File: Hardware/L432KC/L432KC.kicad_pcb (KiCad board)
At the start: 2 copper layers, 64.8 x 55.9 mm, 26 parts, among them J1 Conn_01x09, J2 Conn_01x07, J3 USB_B_Micro, J4 JVCC, J5 JTAG, J6 LogicAna, U1 NUCLEO-L432KC

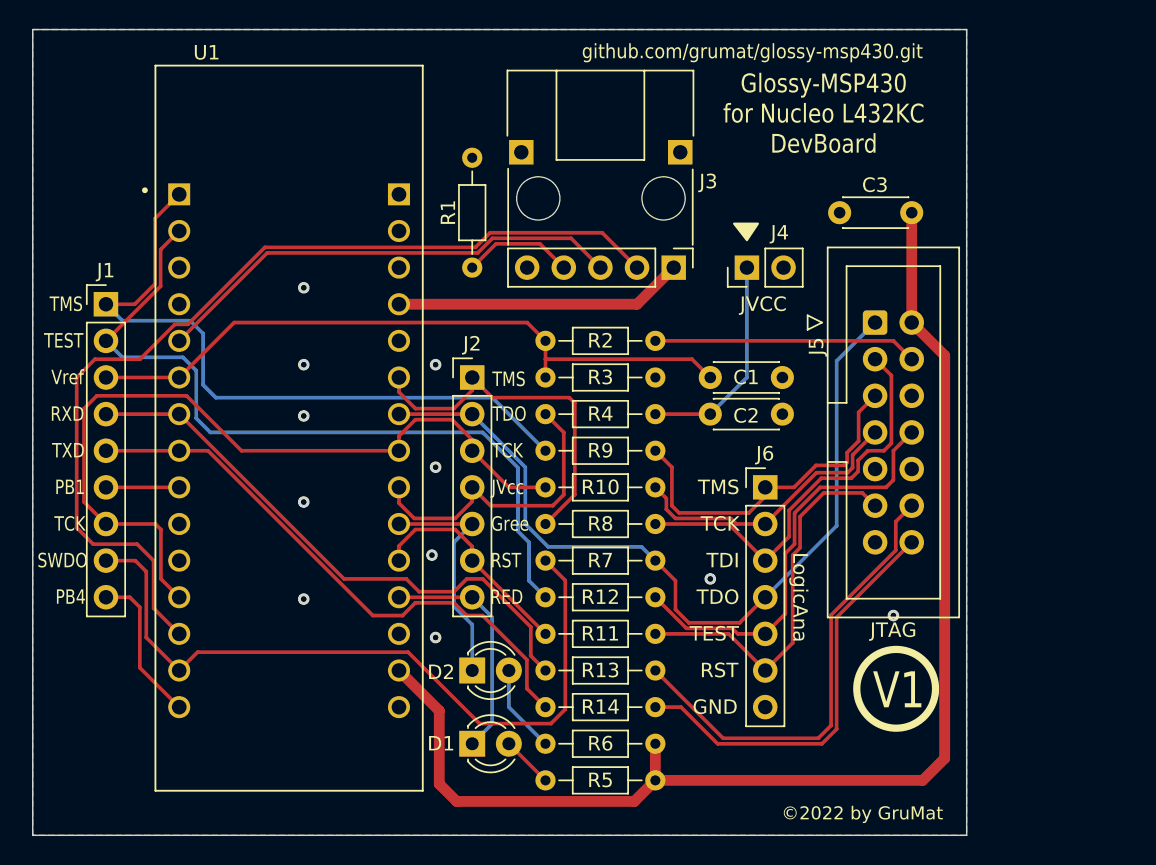
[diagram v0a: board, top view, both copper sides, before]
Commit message: Update Hardware models - Added dual support for L432KC.
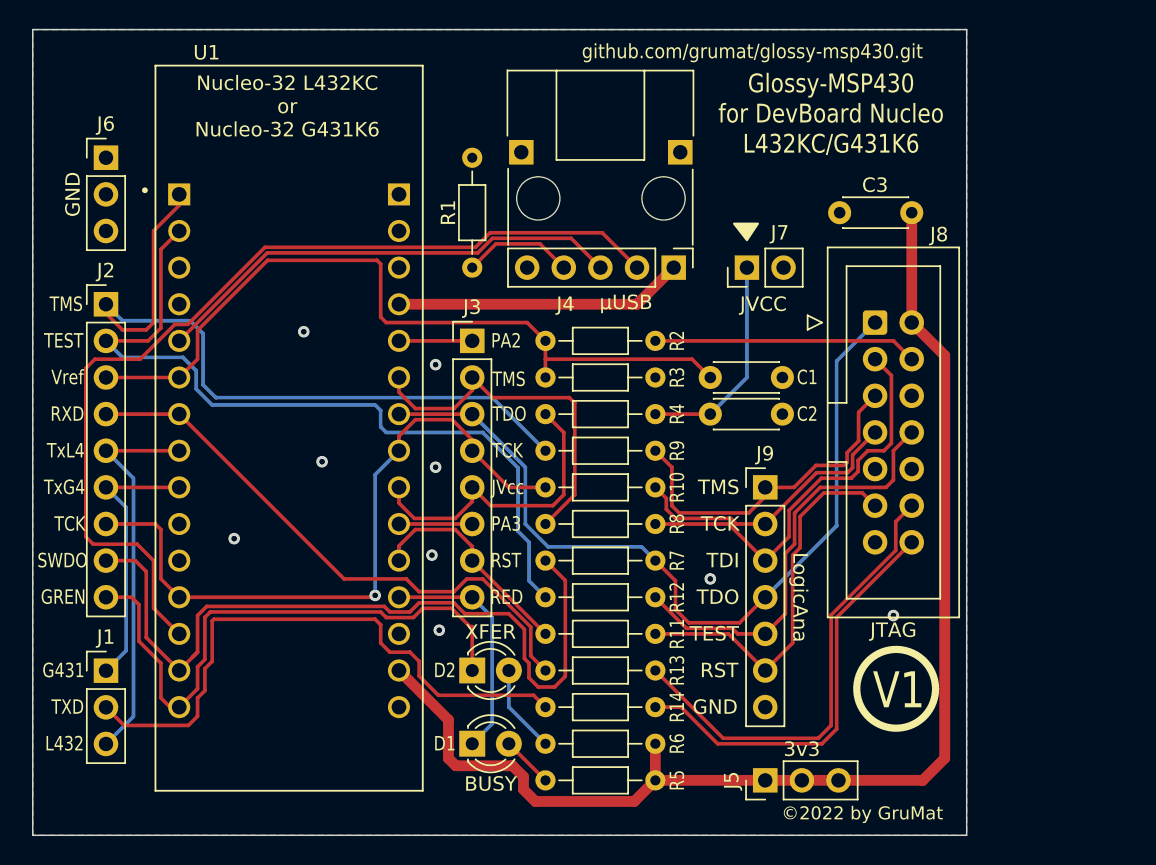
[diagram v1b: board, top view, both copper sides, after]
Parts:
- added J1: L4_G4, Connector_PinHeader_2.54mm:PinHeader_1x03_P2.54mm_Vertical, F.Cu at (106.7, 119.4)
- added J5: 3v3, Connector_PinHeader_2.54mm:PinHeader_1x03_P2.54mm_Vertical, F.Cu at (152.4, 127.0)
- added J6: 3v3, Connector_PinHeader_2.54mm:PinHeader_1x03_P2.54mm_Vertical, F.Cu at (106.7, 83.8)
- J3: renamed from J2; value Conn_01x07 -> Conn_01x08; footprint Connector_PinHeader_2.54mm:PinHeader_1x07_P2.54mm_Vertical -> Connector_PinHeader_2.54mm:PinHeader_1x08_P2.54mm_Vertical
- moved J3 2.54 mm to (132.1, 96.5)
- renumbered J1 to J2, J3 to J4, J4 to J7, J5 to J8, J6 to J9
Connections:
- net /PB1 renamed /TXD_G4
- J2 pad 5: /mTXD -> /TXD_L4
- J2 pad 9: /PB4 -> /LED_GR
- J3 pad 1: /mTDI -> /PA2
- J3 pad 2: /JTDO -> /mTDI
- J3 pad 3: /mTCK -> /JTDO
- J3 pad 4: /mJVCC -> /mTCK
- J3 pad 5: /LED_GR -> /mJVCC
- J3 pad 6: /mRST -> /PA3
- J3 pad 7: /LED_RED -> /mRST
- U1 pad CN3_15: /PB4 -> /LED_GR
- U1 pad CN3_8: /mTXD -> /TXD_L4
- U1 pad CN4_10: /LED_GR -> /PA3
- U1 pad CN4_5: unconnected-(U1-PadCN4_5) -> /PA2
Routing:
- net /TXD_L4: track 0.00 -> 27.0 mm
- net /LED_GR: track 16.3 -> 40.8 mm
- net /TXD_G4: track 5.08 -> 19.0 mm
- net /PB4: track 10.7 -> 0.00 mm
- net /mTCK: track 55.7 -> 47.6 mm, vias 0 -> 1
- net /VREF_2: track 47.1 -> 54.0 mm
- net /PA3: track 0.00 -> 5.08 mm
- net /PA2: track 0.00 -> 5.08 mm
- net /SWDO: track 51.6 -> 55.0 mm
- net /mTMS: track 47.7 -> 51.0 mm
- net /mTXD: track 39.8 -> 41.2 mm
- net /mTEST: track 53.6 -> 54.8 mm
- net +3.3V: track 87.2 -> 86.3 mm
- net /USB_DM: track 66.5 -> 66.0 mm
- net GND: vias 11 -> 9
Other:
- board text added: "3v3"
- board text added: "BUSY"
- board text added: "G431"
- board text added: "GREN"
- board text added: "Glossy-MSP430 for DevBoard Nucleo L432KC/G431K6"
- board text added: "L432"
- board text added: "Nucleo-32 L432KC or Nucleo-32 G431K6"
- board text added: "PA2"
- board text added: "PA3"
- board text added: "TxG4"
- board text added: "TxL4"
- board text added: "XFER"
- board text added: "µUSB"
- board text removed: "Glossy-MSP430 for Nucleo L432KC DevBoard"
- board text removed: "Gree"
- board text removed: "PB1"
- board text removed: "PB4"

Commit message: Improved JTAG bus impedance for BlackPill. Various enhancements for Nucleo K432KC. Added SpiBiWire Adapter.
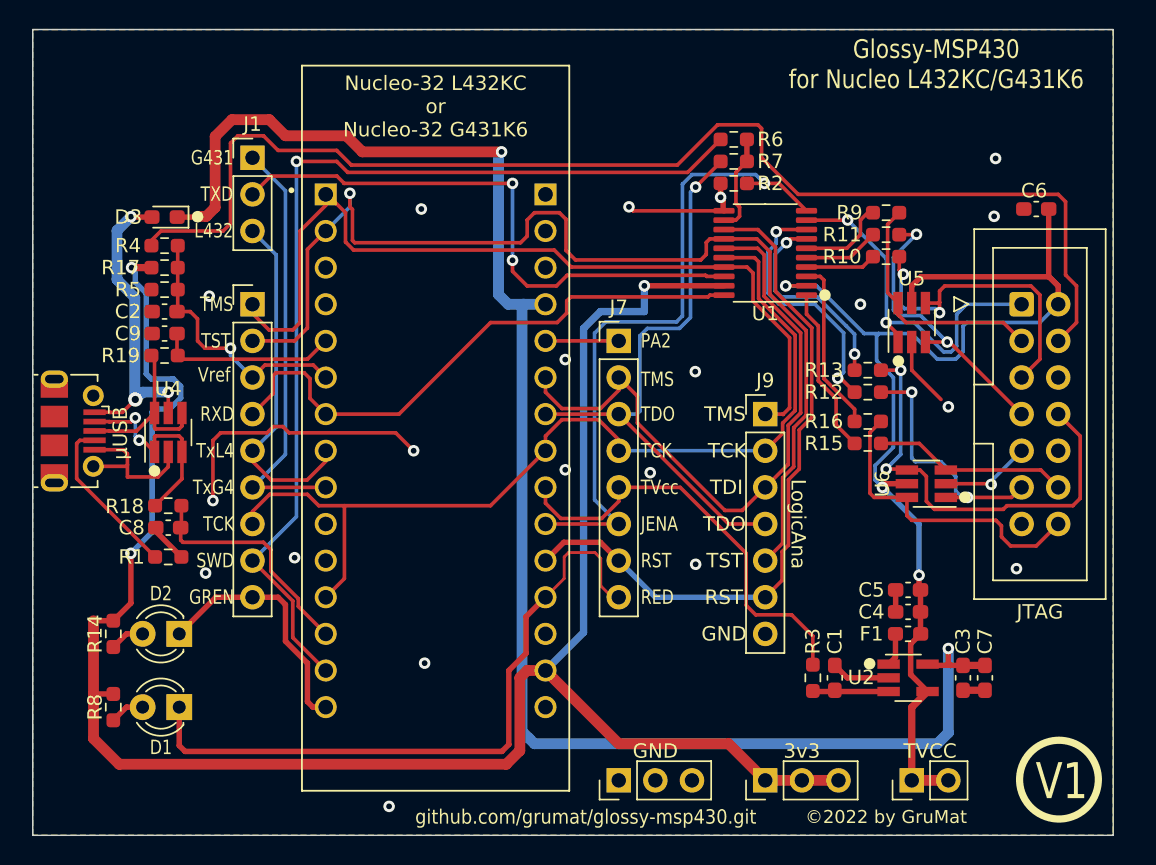
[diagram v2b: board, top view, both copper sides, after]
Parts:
- removed the J4 at (146.1, 91.4)
- added C3: 10uF, Capacitor_SMD:C_0603_1608Metric_Pad1.08x0.95mm_HandSolder, F.Cu at (166.1, 119.9)
- added C4: 10uF, Capacitor_SMD:C_0603_1608Metric_Pad1.08x0.95mm_HandSolder, F.Cu at (162.3, 115.3)
- added C5: 100nF, Capacitor_SMD:C_0603_1608Metric_Pad1.08x0.95mm_HandSolder, F.Cu at (162.3, 113.8)
- added C7: 100nF, Capacitor_SMD:C_0603_1608Metric_Pad1.08x0.95mm_HandSolder, F.Cu at (167.6, 119.9)
- added C8: 33p, Capacitor_SMD:C_0603_1608Metric_Pad1.08x0.95mm_HandSolder, F.Cu at (111.0, 109.5)
- added C9: 33p, Capacitor_SMD:C_0603_1608Metric_Pad1.08x0.95mm_HandSolder, F.Cu at (110.7, 96.0)
- added D3: NSR20F30NXT5G, Diode_SMD:D_0603_1608Metric_Pad1.05x0.95mm_HandSolder, F.Cu at (110.7, 87.9)
- added F1: 0603L010YR, Fuse:Fuse_0603_1608Metric_Pad1.05x0.95mm_HandSolder, F.Cu at (162.3, 116.8)
- added J2: USB_B_Micro, lib:USB_Micro-B_Molex-105017-0001-handsolder, F.Cu at (104.3, 102.8)
- added R17: 470K, Resistor_SMD:R_0603_1608Metric_Pad0.98x0.95mm_HandSolder, F.Cu at (110.7, 91.4)
- added R18: 22, Resistor_SMD:R_0603_1608Metric_Pad0.98x0.95mm_HandSolder, F.Cu at (111.0, 108.0)
- added R19: 22, Resistor_SMD:R_0603_1608Metric_Pad0.98x0.95mm_HandSolder, F.Cu at (110.7, 97.5)
- added R2: 47K, Resistor_SMD:R_0603_1608Metric_Pad0.98x0.95mm_HandSolder, F.Cu at (150.2, 85.6)
- added R7: 22, Resistor_SMD:R_0603_1608Metric_Pad0.98x0.95mm_HandSolder, F.Cu at (150.2, 84.1)
- added U1: TXS0108EPW, Package_SO:TSSOP-20_4.4x6.5mm_P0.65mm, F.Cu at (152.4, 90.4)
- added U2: AD8531ARTZ, Package_TO_SOT_SMD:SOT-23-5_HandSoldering, F.Cu at (162.3, 119.9)
- added U4: SRV05-4, Package_TO_SOT_SMD:SOT-23-6_Handsoldering, F.Cu at (111.0, 102.9)
- added U5: SRV05-4, Package_TO_SOT_SMD:SOT-23-6_Handsoldering, F.Cu at (162.6, 95.2)
- added U6: SRV05-4, Package_TO_SOT_SMD:SOT-23-6_Handsoldering, F.Cu at (163.6, 106.4)
- C1: renamed from C2; footprint Capacitor_THT:C_Disc_D4.3mm_W1.9mm_P5.00mm -> Capacitor_SMD:C_0603_1608Metric_Pad1.08x0.95mm_HandSolder
- C2: renamed from C1; footprint Capacitor_THT:C_Disc_D4.3mm_W1.9mm_P5.00mm -> Capacitor_SMD:C_0603_1608Metric_Pad1.08x0.95mm_HandSolder
- C6: renamed from C3; footprint Capacitor_THT:C_Disc_D4.3mm_W1.9mm_P5.00mm -> Capacitor_SMD:C_0603_1608Metric_Pad1.08x0.95mm_HandSolder
- J5: renamed from J6; value 3v3 -> GND
- J8: renamed from J7; value JVCC -> TVCC
- R1: footprint Resistor_THT:R_Axial_DIN0204_L3.6mm_D1.6mm_P7.62mm_Horizontal -> Resistor_SMD:R_0603_1608Metric_Pad0.98x0.95mm_HandSolder
- R10: renamed from R9; value 100 -> 47; footprint Resistor_THT:R_Axial_DIN0204_L3.6mm_D1.6mm_P7.62mm_Horizontal -> Resistor_SMD:R_0603_1608Metric_Pad0.98x0.95mm_HandSolder
- R11: renamed from R10; value 100 -> 47; footprint Resistor_THT:R_Axial_DIN0204_L3.6mm_D1.6mm_P7.62mm_Horizontal -> Resistor_SMD:R_0603_1608Metric_Pad0.98x0.95mm_HandSolder
- R12: renamed from R11; footprint Resistor_THT:R_Axial_DIN0204_L3.6mm_D1.6mm_P7.62mm_Horizontal -> Resistor_SMD:R_0603_1608Metric_Pad0.98x0.95mm_HandSolder
- R13: renamed from R12; footprint Resistor_THT:R_Axial_DIN0204_L3.6mm_D1.6mm_P7.62mm_Horizontal -> Resistor_SMD:R_0603_1608Metric_Pad0.98x0.95mm_HandSolder
- R14: renamed from R6; footprint Resistor_THT:R_Axial_DIN0204_L3.6mm_D1.6mm_P7.62mm_Horizontal -> Resistor_SMD:R_0603_1608Metric_Pad0.98x0.95mm_HandSolder
- R15: renamed from R13; footprint Resistor_THT:R_Axial_DIN0204_L3.6mm_D1.6mm_P7.62mm_Horizontal -> Resistor_SMD:R_0603_1608Metric_Pad0.98x0.95mm_HandSolder
- R16: renamed from R14; footprint Resistor_THT:R_Axial_DIN0204_L3.6mm_D1.6mm_P7.62mm_Horizontal -> Resistor_SMD:R_0603_1608Metric_Pad0.98x0.95mm_HandSolder
- R3: renamed from R4; footprint Resistor_THT:R_Axial_DIN0204_L3.6mm_D1.6mm_P7.62mm_Horizontal -> Resistor_SMD:R_0603_1608Metric_Pad0.98x0.95mm_HandSolder
- R4: renamed from R2; value 10K -> 4K7; footprint Resistor_THT:R_Axial_DIN0204_L3.6mm_D1.6mm_P7.62mm_Horizontal -> Resistor_SMD:R_0603_1608Metric_Pad0.98x0.95mm_HandSolder
- R5: renamed from R3; value 10K -> 4K7; footprint Resistor_THT:R_Axial_DIN0204_L3.6mm_D1.6mm_P7.62mm_Horizontal -> Resistor_SMD:R_0603_1608Metric_Pad0.98x0.95mm_HandSolder
- R6: renamed from R7; footprint Resistor_THT:R_Axial_DIN0204_L3.6mm_D1.6mm_P7.62mm_Horizontal -> Resistor_SMD:R_0603_1608Metric_Pad0.98x0.95mm_HandSolder
- R8: renamed from R5; footprint Resistor_THT:R_Axial_DIN0204_L3.6mm_D1.6mm_P7.62mm_Horizontal -> Resistor_SMD:R_0603_1608Metric_Pad0.98x0.95mm_HandSolder
- R9: renamed from R8; value 100 -> 47; footprint Resistor_THT:R_Axial_DIN0204_L3.6mm_D1.6mm_P7.62mm_Horizontal -> Resistor_SMD:R_0603_1608Metric_Pad0.98x0.95mm_HandSolder
- moved J5 55.9 mm to (142.2, 127.0), turned to 90 degrees
- moved C2 38.1 mm to (110.7, 94.5), turned to 180 degrees
- moved J8 37.4 mm to (162.6, 127.0)
- moved J1 37.0 mm to (116.8, 83.8)
- moved R1 34.8 mm to (111.0, 111.5), turned to 180 degrees
- moved R5 34.6 mm to (110.7, 93.0), turned to 0 degrees
- moved R9 32.0 mm to (160.8, 87.6)
- moved R6 32.0 mm to (150.2, 82.5), turned to 180 degrees
- moved R14 30.9 mm to (107.2, 116.8), turned to 90 degrees
- moved R8 30.4 mm to (107.2, 121.9), turned to 90 degrees
- moved R11 29.4 mm to (160.8, 89.2)
- moved R12 27.9 mm to (159.5, 100.1)
- moved R13 27.3 mm to (159.5, 98.6)
- moved R4 27.2 mm to (110.7, 89.9), turned to 180 degrees
- moved R10 27.2 mm to (160.8, 90.7)
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- renumbered J8 to J3, J5 to J4, J2 to J6, J3 to J7, U1 to U3
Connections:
- net /PA3 renamed /JENA
- net /mJVCC renamed /mTVCC
- C1 pad 1: /JVCC -> Net-(C1-Pad1)
- C6 pad 1: +3.3V -> /TVCC
- J3 pad 2: +3.3V -> /TVCC
- J3 pad 4: /TVCC -> /TVref
- J7 pad 3: /JTDO -> /mTDO
- J8 pad 1: /JVCC -> /TVCC
- J8 pad 2: GND -> /TVCC
- J9 pad 1: /JTMS -> /mTMS
- J9 pad 2: /JTCK -> /mTCK
- J9 pad 3: /JTDI -> /mTDI
- J9 pad 4: /JTDO -> /mTDO
- J9 pad 5: /JTEST -> /mTEST
- J9 pad 6: /JRST -> /mRST
- R10 pad 1: /mTMS -> /LTMS
- R11 pad 1: /mTCK -> /LTCK
- R12 pad 1: /mRST -> /LRST
- R13 pad 1: /mTEST -> /LTEST
- R15 pad 2: /mRXD -> /LRXD
- R16 pad 2: /mTXD -> /LTXD
- R3 pad 1: /JVCC -> Net-(C1-Pad1)
- R4 pad 2: /TVCC -> /TVref
- R6 pad 1: /SWDO -> Net-(R6-Pad1)
- R6 pad 2: /JTDO -> /SWDO
- R9 pad 1: /mTDI -> /LTDI
- U3 pad CN4_7: /JTDO -> /mTDO
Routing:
- net +5V: track 20.1 -> 113.6 mm, vias 0 -> 2
- net /TVref: track 0.00 -> 85.9 mm
- net /TVCC: track 18.3 -> 82.8 mm, vias 0 -> 3
- net GND: track 0.00 -> 59.5 mm, vias 9 -> 21
- net +3.3V: track 86.3 -> 139.6 mm, vias 0 -> 3
- net /USB_DM: track 66.0 -> 16.4 mm
- net /mTDO: track 0.00 -> 40.9 mm, vias 0 -> 1
- net /JENA: track 5.08 -> 45.9 mm, vias 0 -> 1
- net /VREF_2: track 54.0 -> 18.7 mm, vias 0 -> 1
- net /mRST: track 15.2 -> 48.1 mm
- net /JTDO: track 57.8 -> 25.7 mm, vias 0 -> 2
- net /LED_RED: track 16.4 -> 46.8 mm
- net /LED_GR: track 40.8 -> 17.4 mm
- net VBUS: track 0.00 -> 22.2 mm, vias 0 -> 3
- net /mTEST: track 54.8 -> 76.3 mm, vias 0 -> 1
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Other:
- board size 64.8 x 55.9 mm -> 74.9 x 55.9 mm
- board text added: "Glossy-MSP430 for Nucleo L432KC/G431K6"
- board text added: "JENA"
- board text added: "SWD"
- board text added: "TST"
- board text added: "TVCC"
- board text added: "TVcc"
- board text removed: "BUSY"
- board text removed: "Glossy-MSP430 for DevBoard Nucleo L432KC/G431K6"
- board text removed: "JVCC"
- board text removed: "JVcc"
- board text removed: "PA3"
- board text removed: "SWDO"
- board text removed: "TEST"
- board text removed: "XFER"

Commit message: Files for PCB Manufacturing of 4 boards. Preparation for Board documentation
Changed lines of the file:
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@@
     (aux_axis_origin 101.6 74.93)
     (pcbplotparams
-      (layerselection 0x00010fc_ffffffff)
+      (layerselection 0x00010a8_7fffffff)
       (disableapertmacros false)
-      (usegerberextensions false)
-      (usegerberattributes true)
-      (usegerberadvancedattributes true)
-      (creategerberjobfile true)
+      (usegerberextensions true)
+      (usegerberattributes false)
+      (usegerberadvancedattributes false)
+      (creategerberjobfile false)
       (svguseinch false)
       (svgprecision 6)
@@
       (psa4output false)
       (plotreference true)
-      (plotvalue true)
+      (plotvalue false)
       (plotinvisibletext false)
       (sketchpadsonfab false)
-      (subtractmaskfromsilk false)
-      (outputformat 1)
+      (subtractmaskfromsilk true)
+      (outputformat 5)
       (mirror false)
-      (drillshape 1)
+      (drillshape 0)
       (scaleselection 1)
-      (outputdirectory "")
+      (outputdirectory "output/")
     )
   )
@@
     (fp_line (start 4.52 19.15) (end -1.98 19.15) (layer "F.Fab") (width 0.1))
     (fp_line (start -1.98 9.67) (end -1.98 9.67) (layer "F.Fab") (width 0.1))
-    (pad "1" thru_hole roundrect (at 0 0) (size 1.7 1.7) (drill 1) (layers *.Cu *.Mask) (roundrect_rratio 0.147059)
+    (pad "1" thru_hole roundrect (at 0 0) (size 1.7 1.7) (drill 1) (layers *.Cu *.Mask) (roundrect_rratio 0.1470588235)
       (net 3 "/JTDO") (pinfunction "Pin_1") (pintype "passive"))
     (pad "2" thru_hole circle (at 2.54 0) (size 1.7 1.7) (drill 1) (layers *.Cu *.Mask)
@@
       (net 51 "unconnected-(U3-PadCN4_15)") (pinfunction "PB3") (pintype "power_in+no_connect"))
     (model "${KIPRJMOD}/lib/MB1430-G431KBT6-A02.step"
-      (offset (xyz -9.2 -25.2 7))
+      (offset (xyz -9.2 -25.2 11.5))
+      (scale (xyz 1 1 1))
+      (rotate (xyz 0 0 0))
+    )
+    (model "${KICAD6_3DMODEL_DIR}/Connector_PinSocket_2.54mm.3dshapes/PinSocket_1x16_P2.54mm_Vertical.wrl"
+      (offset (xyz -7.6 18.75 0))
+      (scale (xyz 1 1 1))
+      (rotate (xyz 0 0 0))
+    )
+    (model "${KICAD6_3DMODEL_DIR}/Connector_PinSocket_2.54mm.3dshapes/PinSocket_1x16_P2.54mm_Vertical.wrl"
+      (offset (xyz 7.5 18.75 0))
       (scale (xyz 1 1 1))
       (rotate (xyz 0 0 0))
@@
     (effects (font (size 1 1) (thickness 0.15)))
   )
+  (target plus (at 101.6 73.66) (size 5) (width 0.05) (layer "Edge.Cuts"))
+  (target plus (at 116.84 83.82) (size 5) (width 0.05) (layer "Edge.Cuts"))
   (segment (start 109.8315 91.44) (end 108.458 91.44) (width 0.508) (layer "F.Cu") (net 1))
   (segment (start 105.8145 121.0075) (end 105.8145 124.1025) (width 0.75) (layer "F.Cu") (net 1))

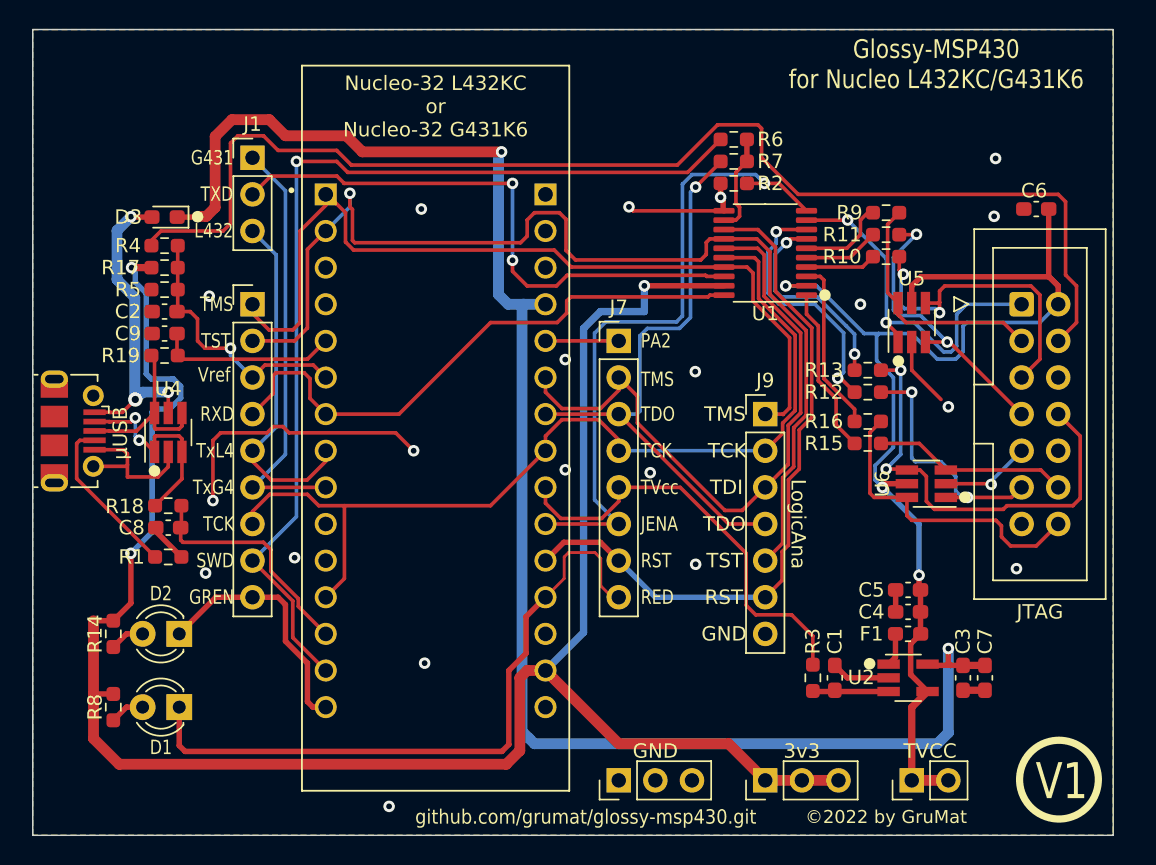
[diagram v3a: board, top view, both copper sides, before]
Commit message: Swapped LRXD and LTXD on both prototype boards.
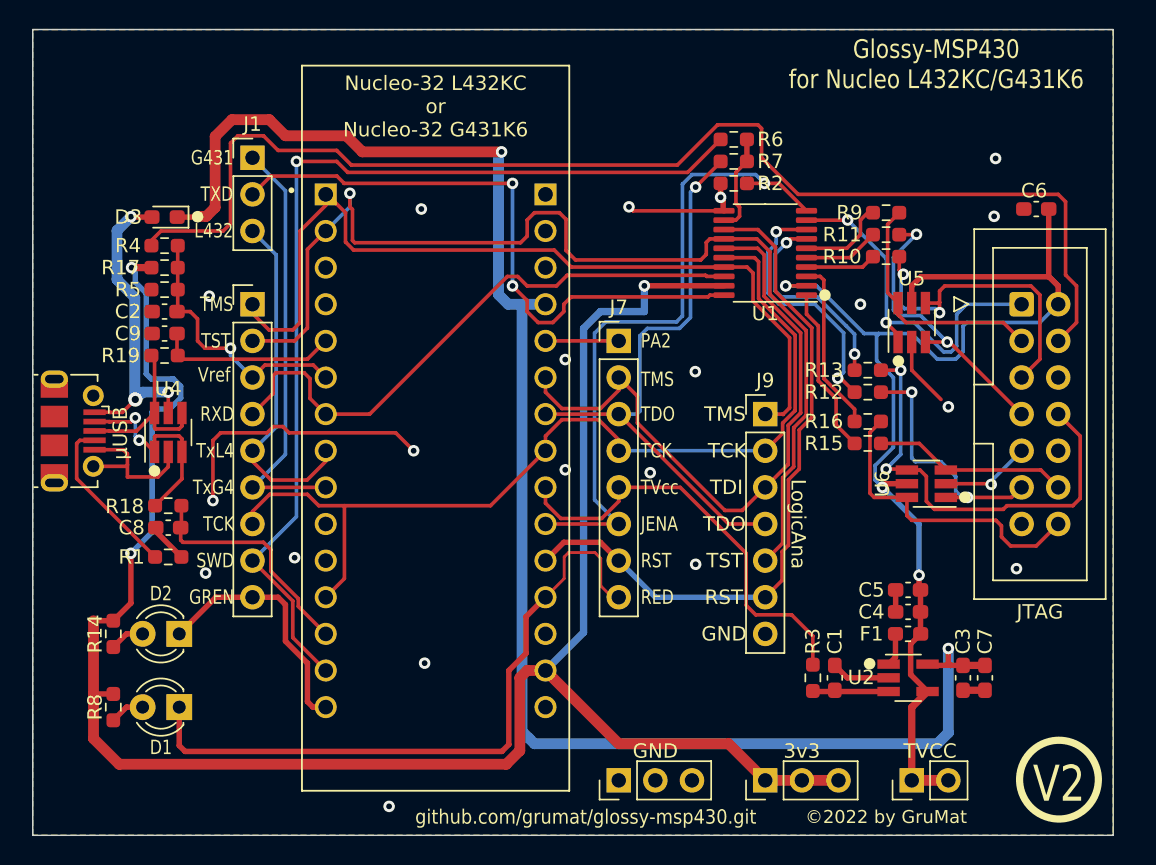
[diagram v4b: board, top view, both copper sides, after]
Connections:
- R15 pad 2: /LRXD -> /LTXD
- R16 pad 2: /LTXD -> /LRXD
- U1 pad 1: /LRXD -> /LTXD
- U1 pad 18: /mTXD -> /mRXD
- U1 pad 20: /mRXD -> /mTXD
- U1 pad 3: /LTXD -> /LRXD
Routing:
- net /mTXD: track 40.3 -> 43.1 mm
- net /mRXD: track 40.5 -> 41.2 mm
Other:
- board text added: "V2"
- board text removed: "V1"
